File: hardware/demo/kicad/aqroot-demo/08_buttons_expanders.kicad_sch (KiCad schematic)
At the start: 30 parts, among them SW2 A_SELECT, SW3 UP, SW4 DOWN, SW5 LEFT, SW6 RIGHT, SW7 B_BACK, U2 PCAL9535APW, U3 PCAL9535APW

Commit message: demo: D-742 -- the owner decision on U11.3 is SPENT, and reading the datasheet to spend it found that this board's charger status decode was INVERTED on STAT1.
The owner approved (2026-09-17) leaving /BQ25185_STAT2's U11.3 unconnected.  routing_ledger.py now carries APPROVED_UNROUTED, deliberately NOT folded into APPROVED_NC: a J5 NC contact carries no net and is simply not counted, whereas U11.3 carries a real net on a fitted part and is genuinely unrouted.  Folding it in would have deleted the board's record of why the pin is bare AND made neck_contract N2 vacuous, because U11.3 is the only pad N2 compares on this board.  So nets[] keeps telling the copper truth -- retained_open_edges stays 1 -- and the governance verdict is published beside it: approved_unrouted_edges 1, unapproved_open_edges 0.  The declaration is re-proved against the board every run (pad exists, part fitted, net matches, still stranded, R128 and TP7 still fitted) and four non-vacuity controls show it FAILS when any of those stops being true.

Then the datasheet was read, which nobody in this programme had done since 2026-08, and the independent review's pre-fab item "validate STAT1/STAT2 decoding against the current TI truth table" turned out not to be a formality.  THE DECODE THIS BOARD CARRIED WAS INVERTED ON STAT1.  R127/R128's schematic notes and D-170 all said "STAT1 LOW = charging; STAT1 HIGH + STAT2 LOW = fault", citing a "SLUSF65A Table 7-2" that is not a status table.  SLUSF65B section 6.3.10 Table 6-2 says the opposite on both rows: STAT1 LOW is a FAULT, STAT1 HIGH with STAT2 LOW is CHARGING.  The datasheet confirms its own table twice more (section 6.3.7.1's VIN_OVP row, and the flow diagram's "STAT1 and STAT2 to 1" for Charge Done), and its revision history shows TI never changed the table -- this was a reading error made in FBV2-S1-008 and copied ever since.  POWER_FAULT_STATE_TABLE.md had it right the whole time and nothing compared the two.

The correction makes the owner decisi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
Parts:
- R127: Note BQ25185 STAT1 pull-up, FBV2-S1-008. SLUSF65A Table 5-1: STAT1 and STAT2 are OPEN-DRAIN, pull-up resistor 1 kOhm to 20 kOhm, maximum pull-up rail 5 V, 20 mA sink, and either may be left floating if unused. 10 kOhm is inside that window and is chosen over the 20 kOhm of Ruling G for the same reason the button pull-ups are 10 kOhm and not the PCAL internal 100 kOhm: the expander input leaks up to 1 uA and the board will be handled, so a stiffer high is worth 0.33 mA - and that current only flows while the charger is actually holding the pin LOW. CHARGER STATE DECODE, SLUSF65A Table 7-2: STAT1 LOW = charging; STAT1 HIGH with STAT2 LOW = fault; both HIGH is ONE combined state covering charge complete, sleep and charge disabled. WITH NO BATTERY FITTED the device cycles the BAT-pin capacitor and STAT2 TOGGLES while STAT1 stays stable - which is why both pins are landed, and why firmware must leave the STAT2 interrupt mask bit SET and poll instead. -> BQ25185 STAT1 pull-up, FBV2-S1-008. SLUSF65A Table 5-1: STAT1 and STAT2 are OPEN-DRAIN, pull-up resistor 1 kOhm to 20 kOhm, maximum pull-up rail 5 V, 20 mA sink, and either may be left floating if unused. 10 kOhm is inside that window and is chosen over the 20 kOhm of Ruling G for the same reason the button pull-ups are 10 kOhm and not the PCAL internal 100 kOhm: the expander input leaks up to 1 uA and the board will be handled, so a stiffer high is worth 0.33 mA - and that current only flows while the charger is actually holding the pin LOW. *** D-742 CORRECTED THIS NOTE. THE DECODE PRINTED HERE UNTIL 2026-09-18 WAS INVERTED ON STAT1 AND FIRMWARE MUST NOT USE IT. The authority is SLUSF65B (August 2026) section 6.3.10 Table 6-2 'Status Pins State Table' - there is no Table 7-2; section 7 is Application and Implementation. THE CORRECT TABLE IS: STAT1 HIGH + STAT2 HIGH = charge completed, charger in sleep mode, or charge disabled (including VBAT > VRCH). STAT1 HIGH + STAT2 LOW = NORMAL 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
- R128: Note BQ25185 STAT2 pull-up, FBV2-S1-008. Same 10 kOhm to +3V3 as R127 and the same SLUSF65A 1 k to 20 k window. STAT2 carries the fault distinction: STAT1 HIGH with STAT2 LOW is a fault, both HIGH is the combined charge-complete / sleep / charge-disabled state, so STAT1 alone would convey only fault/no-fault. STAT2 is also the pin that toggles continuously when no battery is present, so it is landed on an interrupt-capable PCAL input whose mask bit is SET by hardware default - the PCAL9535A powers up with 4Ah/4Bh = FFh - and firmware must leave it masked and poll. That is what let Ruling G reverse the earlier STAT1-only recommendation without importing a wake storm. -> BQ25185 STAT2 pull-up, FBV2-S1-008. Same 10 kOhm to +3V3 as R127 and the same SLUSF65A 1 k to 20 k window. *** D-742 CORRECTED THIS NOTE TWICE OVER. (1) THE DECODE IT CITED WAS INVERTED ON STAT1 - see R127's note for SLUSF65B Table 6-2 in full. In the real table STAT2 is the pin that separates CHARGING (STAT1 HIGH, STAT2 LOW) from CHARGE-COMPLETE / SLEEP / DISABLED (both HIGH), and it separates a RECOVERABLE fault (STAT1 LOW, STAT2 HIGH) from a NON-RECOVERABLE one (both LOW). It does not carry 'the fault distinction'; STAT1 does. (2) R128 IS RETAINED BUT ITS NET NEVER REACHES THE CHARGER. U11.3 ships UNCONNECTED by owner decision D-742 (2026-09-17): D-734 proved the land has no escape at any manufacturable width and D-741 re-measured the binding window as exactly 0.100 mm, between D-269's clearance to U11.2's BAT escape and U11.4's GND land, against this board's 0.200 mm published floor - a window fixed by the DLH0010A pinout, since BAT is pin 2 and STAT2 pin 3, so it moves with neith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

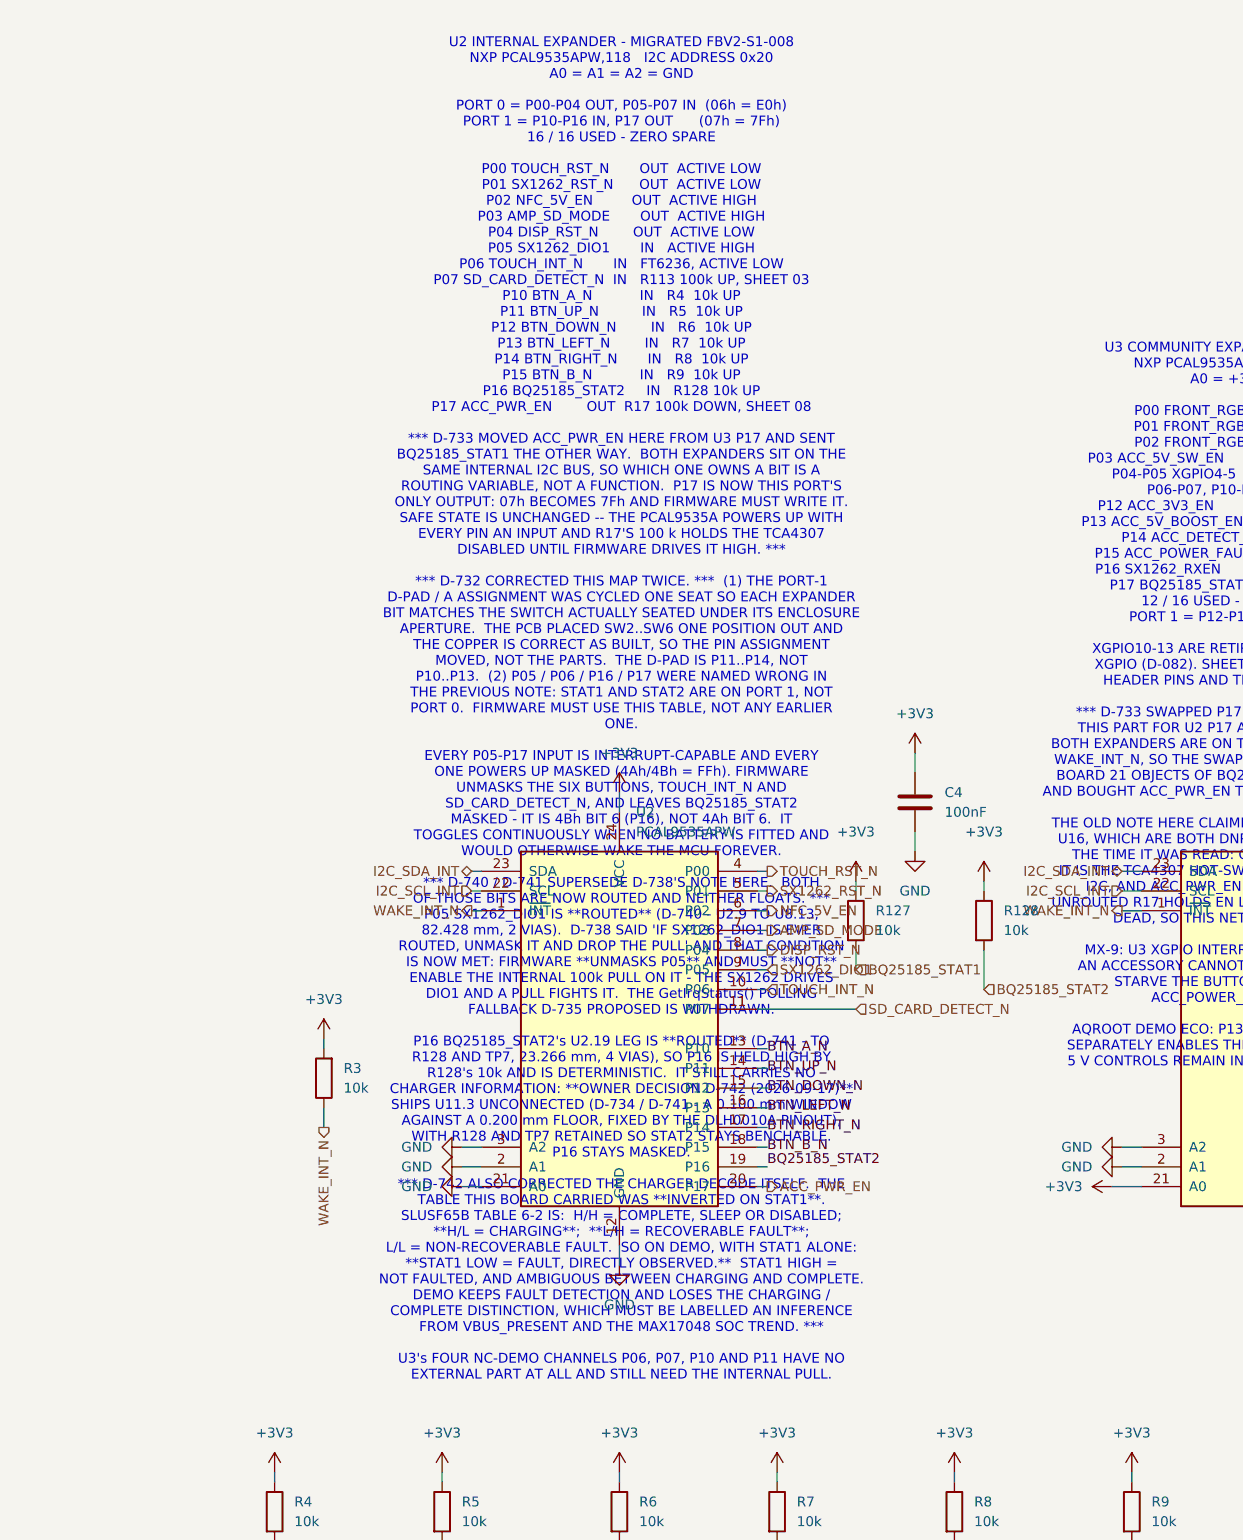
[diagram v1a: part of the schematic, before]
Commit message: demo: D-776 -- the as-built limits told firmware to read a signal this board does not have, and the list of signals it does not have is now computed off the copper
THE GENERATED FIRMWARE MAP'S OWN AS-BUILT LIMITS -- a block headed "facts
firmware cannot discover and must not get wrong" -- told firmware to infer
charging state "from VBUS presence plus the MAX17048 trend".  THERE IS NO
VBUS-PRESENCE SIGNAL ON THIS BOARD.  R104 150k and R105 220k divide
USB_VBUS_CHG to 2.973 V, C68 filters it, all three are FITTED, and
/01_POWER_TREE/VBUS_PRESENT reaches TP31 AND NOTHING ELSE -- no U1 pin, no
U2/U3 bit.  The same sentence stood in 01_power_tree.kicad_sch, in
08_buttons_expanders.kicad_sch and in Firmware/README.md, and the sheet-01
telemetry note added "raw VBUS never reaches the expander", which reads as
though the DIVIDED level does.

TWO MORE OF THE SAME SHAPE WERE UNDECLARED BESIDE IT, found by asking the
question of the whole board instead of one note:

  * /01_POWER_TREE/LTC4368_FAULT_N -- the LATCHING battery breaker's own FAULT
    output, reaching R81, R82, TP18 and Q9's GATE, whose drain is REC_FAULT_B
    and disappears into the autonomous dead-cell recovery chain.  FIRMWARE
    CANNOT OBSERVE THAT THE BATTERY BREAKER HAS TRIPPED.
  * Net-(U12-PG) -- the TPS63020's POWER GOOD, reaching R41 1M and TP8 only.

THE REAL DEFECT IS THAT THE LIST WAS REMEMBERED.  `limits` already carried
FUEL_GAUGE_ALRT_NOT_WIRED and ACC_BUS_READY_NOT_WIRED -- the PATTERN was right
and had been applied twice, BY HAND, so three nets of exactly that shape were
never added and one of them was named by another limit as though readable.

SO THE LIST IS DERIVED.  A net is FIRMWARE-REACHABLE iff it touches a pad of
U1, U2 or U3; BENCH-PROBED iff it touches a TP pad.  gen_firmware_hw_map.py
enumerates every net that is probed and not reachable OFF THE COPPER and
REFUSES TO EMIT if one is undeclared, or if a declaration names a net that has
since been wired -- both directions, which is the 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
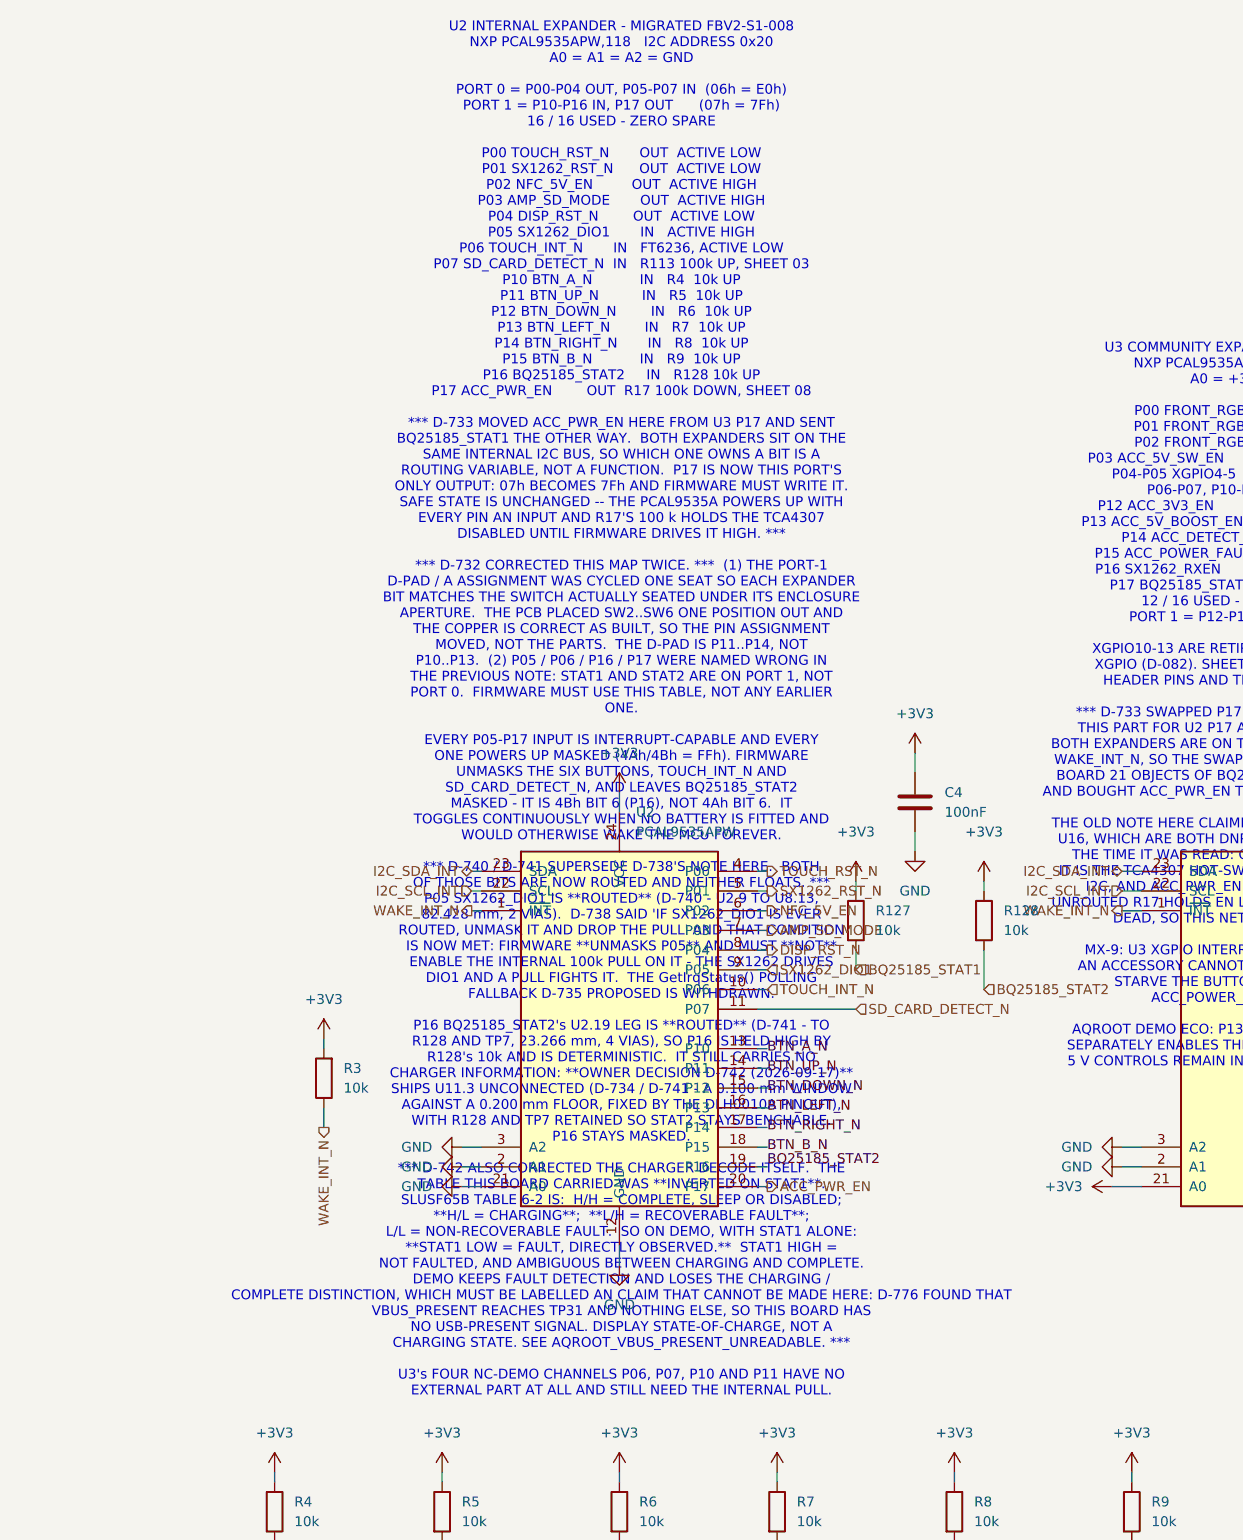
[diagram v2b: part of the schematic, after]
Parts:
- R127: Note BQ25185 STAT1 pull-up, FBV2-S1-008. SLUSF65A Table 5-1: STAT1 and STAT2 are OPEN-DRAIN, pull-up resistor 1 kOhm to 20 kOhm, maximum pull-up rail 5 V, 20 mA sink, and either may be left floating if unused. 10 kOhm is inside that window and is chosen over the 20 kOhm of Ruling G for the same reason the button pull-ups are 10 kOhm and not the PCAL internal 100 kOhm: the expander input leaks up to 1 uA and the board will be handled, so a stiffer high is worth 0.33 mA - and that current only flows while the charger is actually holding the pin LOW. *** D-742 CORRECTED THIS NOTE. THE DECODE PRINTED HERE UNTIL 2026-09-18 WAS INVERTED ON STAT1 AND FIRMWARE MUST NOT USE IT. The authority is SLUSF65B (August 2026) section 6.3.10 Table 6-2 'Status Pins State Table' - there is no Table 7-2; section 7 is Application and Implementation. THE CORRECT TABLE IS: STAT1 HIGH + STAT2 HIGH = charge completed, charger in sleep mode, or charge disabled (including VBAT > VRCH). STAT1 HIGH + STAT2 LOW = NORMAL 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 -> BQ25185 STAT1 pull-up, FBV2-S1-008. SLUSF65A Table 5-1: STAT1 and STAT2 are OPEN-DRAIN, pull-up resistor 1 kOhm to 20 kOhm, maximum pull-up rail 5 V, 20 mA sink, and either may be left floating if unused. 10 kOhm is inside that window and is chosen over the 20 kOhm of Ruling G for the same reason the button pull-ups are 10 kOhm and not the PCAL internal 100 kOhm: the expander input leaks up to 1 uA and the board will be handled, so a stiffer high is worth 0.33 mA - and that current only flows while the charger is actually holding the pin LOW. *** D-742 CORRECTED THIS NOTE. THE DECODE PRINTED HERE UNTIL 2026-09-18 WAS INVERTED ON STAT1 AND FIRMWARE MUST NOT USE IT. The authority is SLUSF65B (August 2026) section 6.3.10 Table 6-2 'Status Pins State Table' - there is no Table 7-2; section 7 is Application and Implementation. THE CORRECT TABLE IS: STAT1 HIGH + STAT2 HIGH = charge completed, charger in sleep mode, or charge disabled (including VBAT > VRCH). STAT1 HIGH + STAT2 LOW = NORMAL 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
